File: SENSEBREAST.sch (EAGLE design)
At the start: 16 parts, among them IC1 BME280, IC2 MCP3202SN, IC3 LSM9DS1, J1 M40-SOCKET-BELOW, J2 Heart Rate

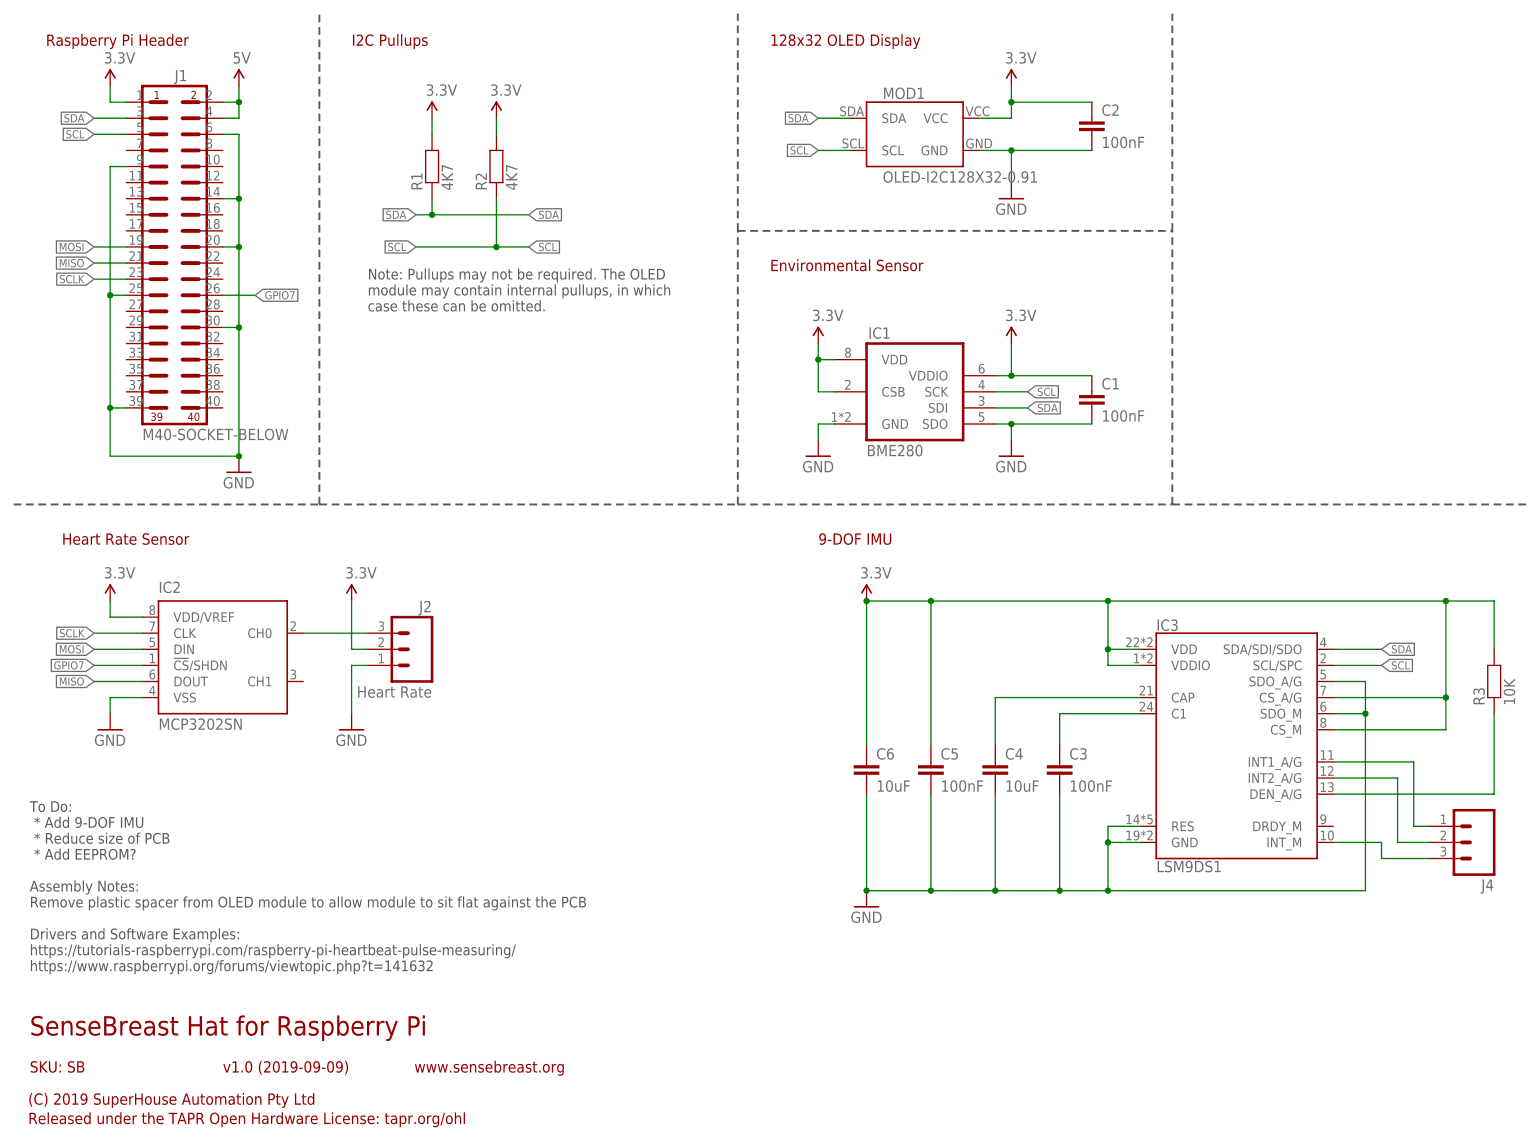
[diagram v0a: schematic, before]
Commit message: Replaced BME280 with BME680 to allow detection of VOC levels in the environment
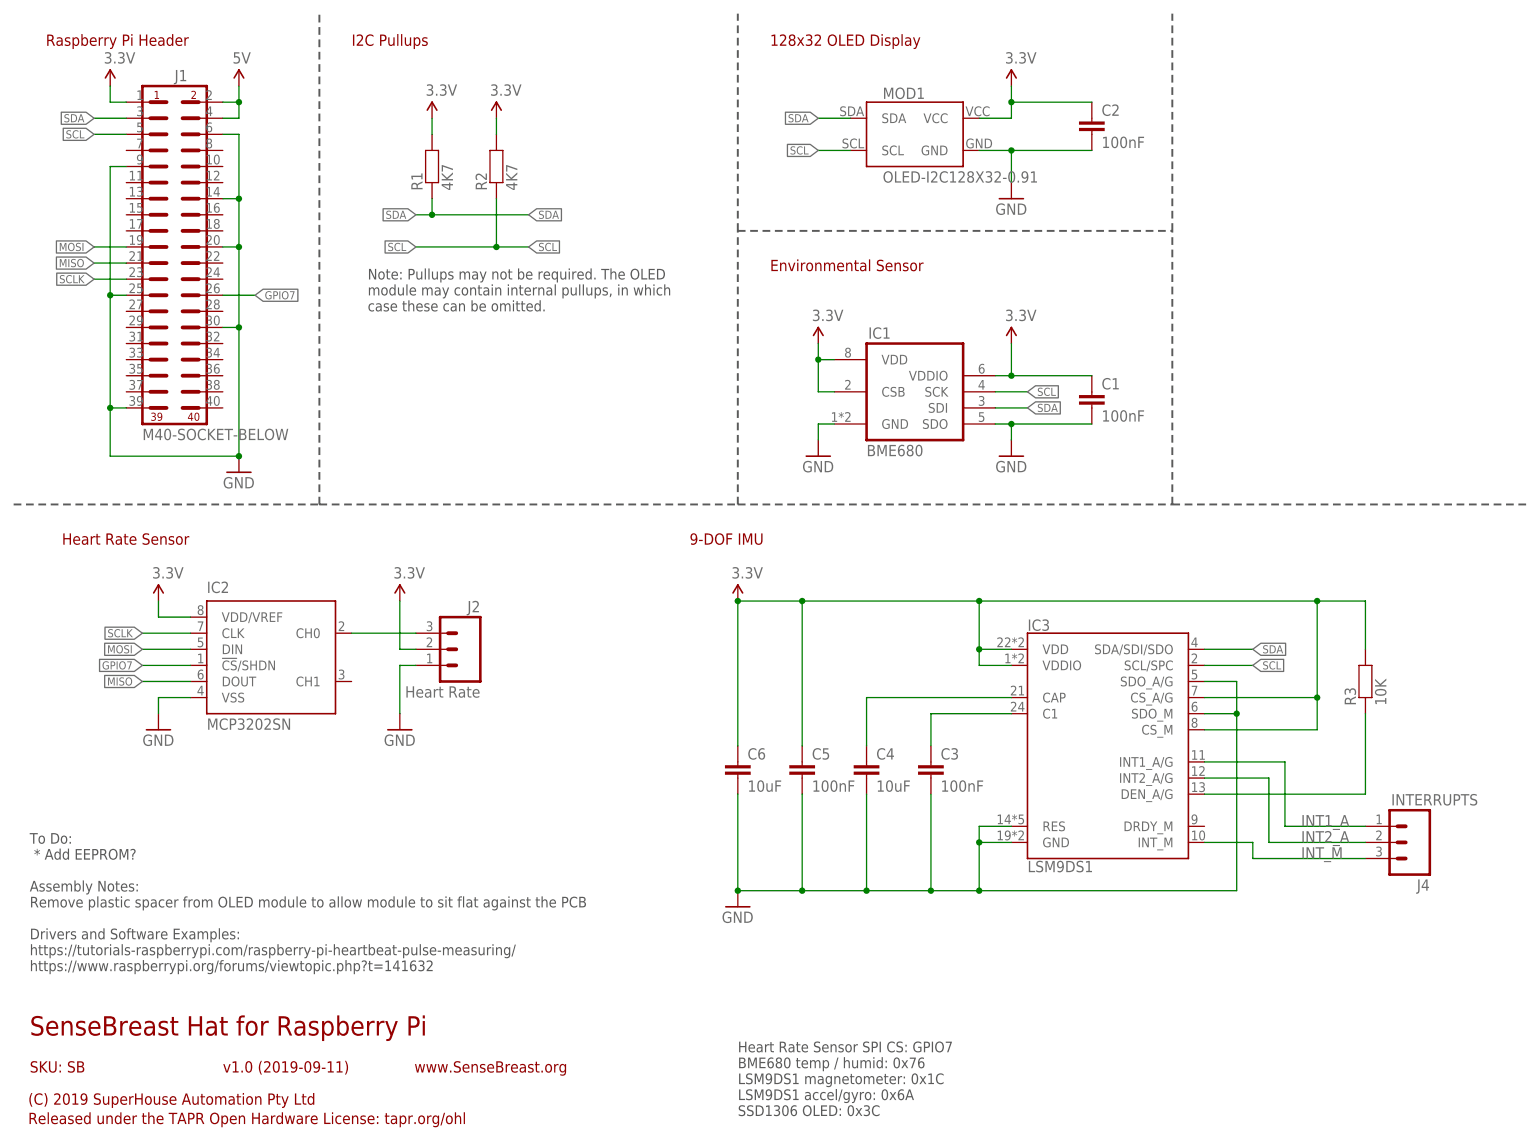
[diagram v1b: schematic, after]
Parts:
- IC1: value BME280 -> BME680; device SuperHouse-Sensors:BME280 -> SuperHouse-Sensors:BME680
- J4: value (none) -> INTERRUPTS
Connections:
- net N$2 renamed INT1_A
- net N$3 renamed INT2_A
- net N$5 renamed INT_M
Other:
- note added: "Heart Rate Sensor SPI CS: GPIO7 BME680 temp / humid: 0x76 LSM9DS1 magnetometer: 0x1C LSM9DS1 accel/gyro: 0x6A SSD1306 OLED: 0x3C"
- note added: "To Do: * Add EEPROM? Assembly Notes: Remove plastic spacer from OLED module to allow module to sit flat against the PCB Drivers and Software Examples: https://tutorials-raspberrypi.com/raspberry-pi-heartbeat-pulse-measuring/ https://www.raspberrypi.org/forums/viewtopic.php?t=141632"
- note added: "v1.0 (2019-09-11)"
- note added: "www.SenseBreast.org"
- note removed: "To Do: * Add 9-DOF IMU * Reduce size of PCB * Add EEPROM? Assembly Notes: Remove plastic spacer from OLED module to allow module to sit flat against the PCB Drivers and Software Examples: https://tutorials-raspberrypi.com/raspberry-pi-heartbeat-pulse-measuring/ https://www.raspberrypi.org/forums/viewtopic.php?t=141632"
- note removed: "v1.0 (2019-09-09)"
- note removed: "www.sensebreast.org"
- moved on the sheet: C3, C4, C5, C6, IC2, IC3, J2, J4, R3

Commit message: Final routing, plus ERC and DRC for v1.0 release
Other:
- note added: "SKU: SENSEBREAST"
- note removed: "SKU: SB"
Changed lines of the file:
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@@
 <frame x1="35.56" y1="12.7" x2="66.04" y2="17.78" columns="8" rows="5" layer="94"/>
 <frame x1="5.08" y1="5.08" x2="116.84" y2="17.78" columns="0" rows="0" layer="94" border-left="no" border-top="no" border-right="no" border-bottom="no"/>
-<text x="7.62" y="14.478" size="1.778" layer="94">SKU: SB</text>
+<text x="7.62" y="14.478" size="1.778" layer="94">SKU: SENSEBREAST</text>
 <text x="10.16" y="176.53" size="1.778" layer="94">Raspberry Pi Header</text>
 <wire x1="53.34" y1="104.14" x2="53.34" y2="181.61" width="0.3048" layer="97" style="longdash"/>
